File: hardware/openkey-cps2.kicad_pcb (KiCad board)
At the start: 2 copper layers, 27.4 x 27.2 mm, 19 parts, among them CN9 Conn_01x06, J1 VCC Pad, J2 CN2, J3 GND Pad, J4 VCC, J5 GND, J6 J5 / UDPI, U1 ATtinyxx4

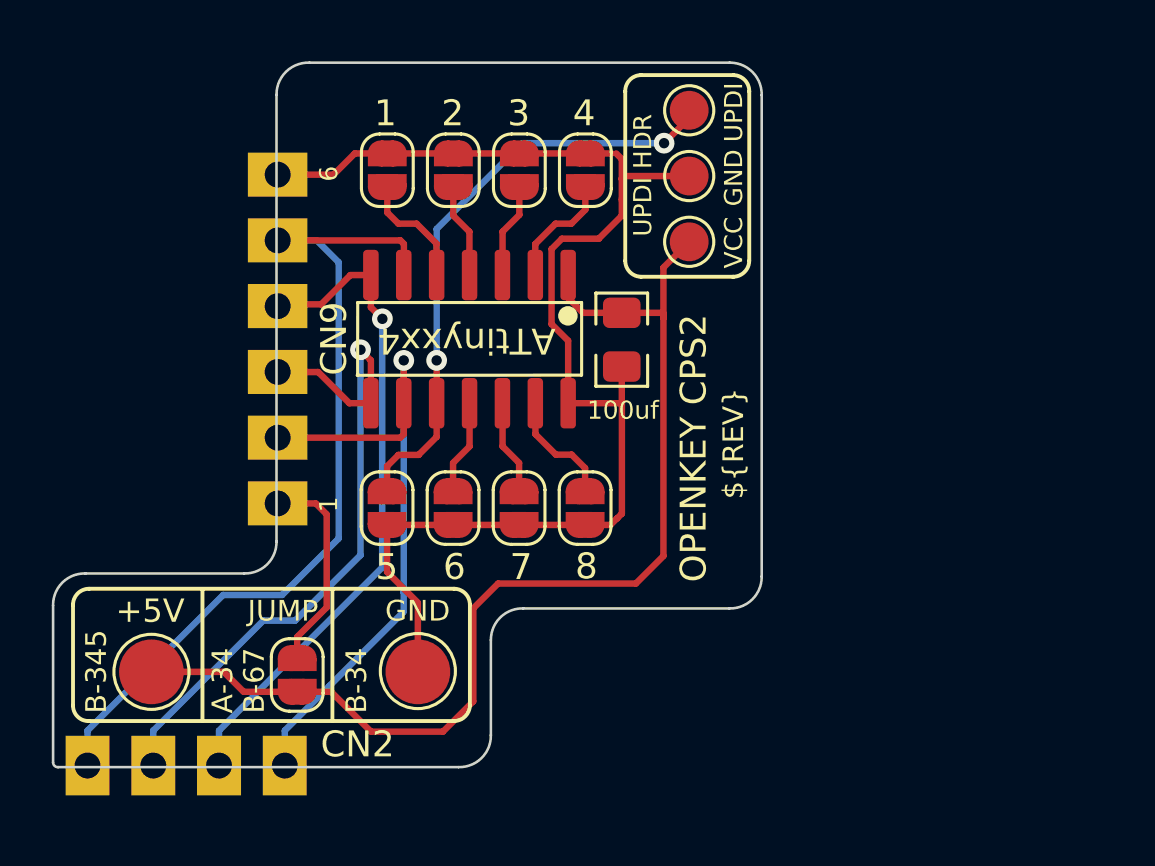
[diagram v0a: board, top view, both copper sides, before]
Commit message: HW: get most everything 0.25mm aligned
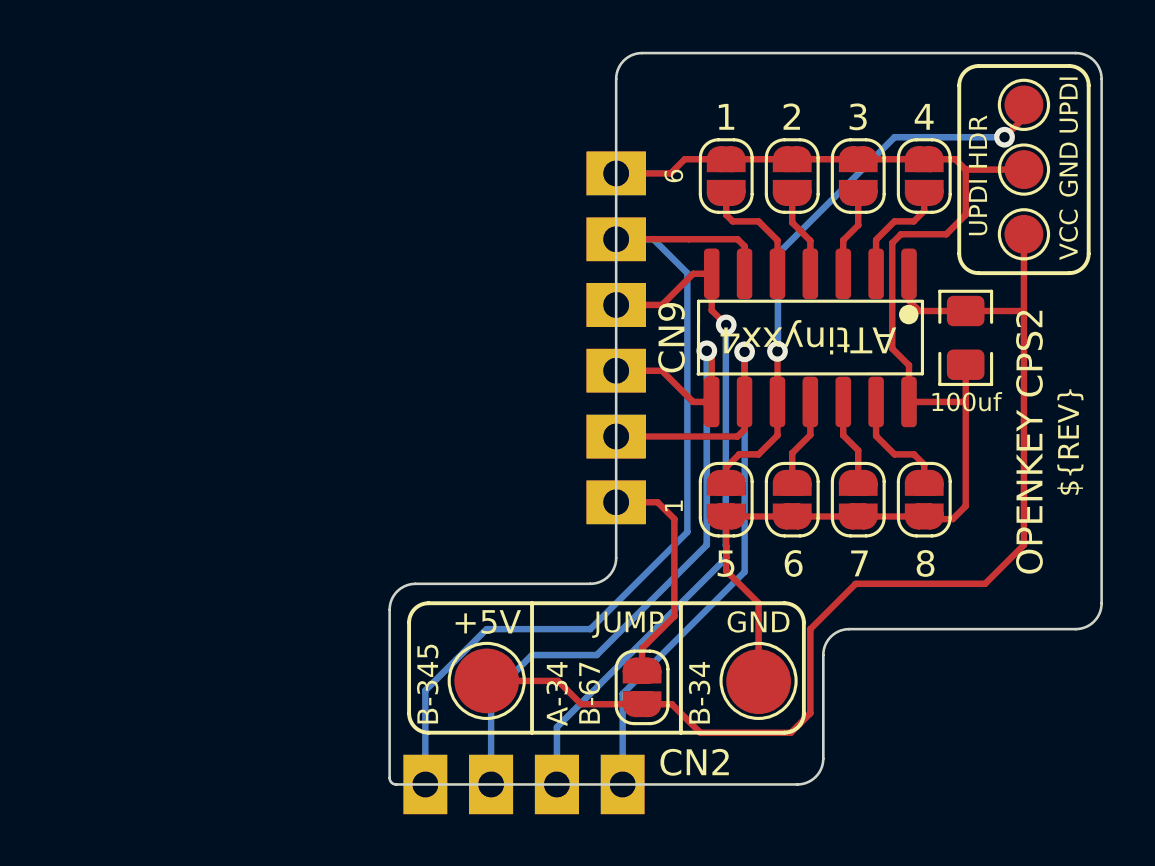
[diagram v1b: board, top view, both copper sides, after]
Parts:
- moved JP9 13.3 mm to (134.0, 110.8)
- moved C1 13.3 mm to (146.5, 97.2)
- moved J3 13.2 mm to (138.5, 110.5)
- moved U1 13.2 mm to (140.5, 97.2)
- moved REF** 13.1 mm to (143.0, 98.0)
- moved JP2 13.1 mm to (139.8, 103.5)
- moved JP1 13.1 mm to (137.2, 103.5)
- moved JP3 13.1 mm to (142.3, 103.5)
- moved JP4 13.1 mm to (144.9, 103.5)
- moved JP7 13.1 mm to (139.8, 91.0)
- moved JP5 13.1 mm to (144.9, 91.0)
- moved JP6 13.1 mm to (142.3, 91.0)
- moved JP8 13.1 mm to (137.2, 91.0)
- moved CN9 13.1 mm to (133.0, 103.6)
- moved J2 13.1 mm to (133.2, 114.5)
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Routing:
- net RESET: track 32.5 -> 35.3 mm
- net GND: track 50.0 -> 51.5 mm
- net SETUP: track 26.3 -> 27.7 mm
- net DATA: track 25.2 -> 26.5 mm
- net VCC: track 43.2 -> 44.1 mm
- net /J5 / UPDI: track 23.2 -> 22.3 mm
- net CLOCK: track 25.7 -> 26.6 mm
- net /CN9 VCC: track 8.01 -> 8.76 mm
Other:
- board size 27.4 x 27.2 mm -> 27.5 x 28.2 mm

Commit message: HW: tweak so a VCC trace isn't so close to edge
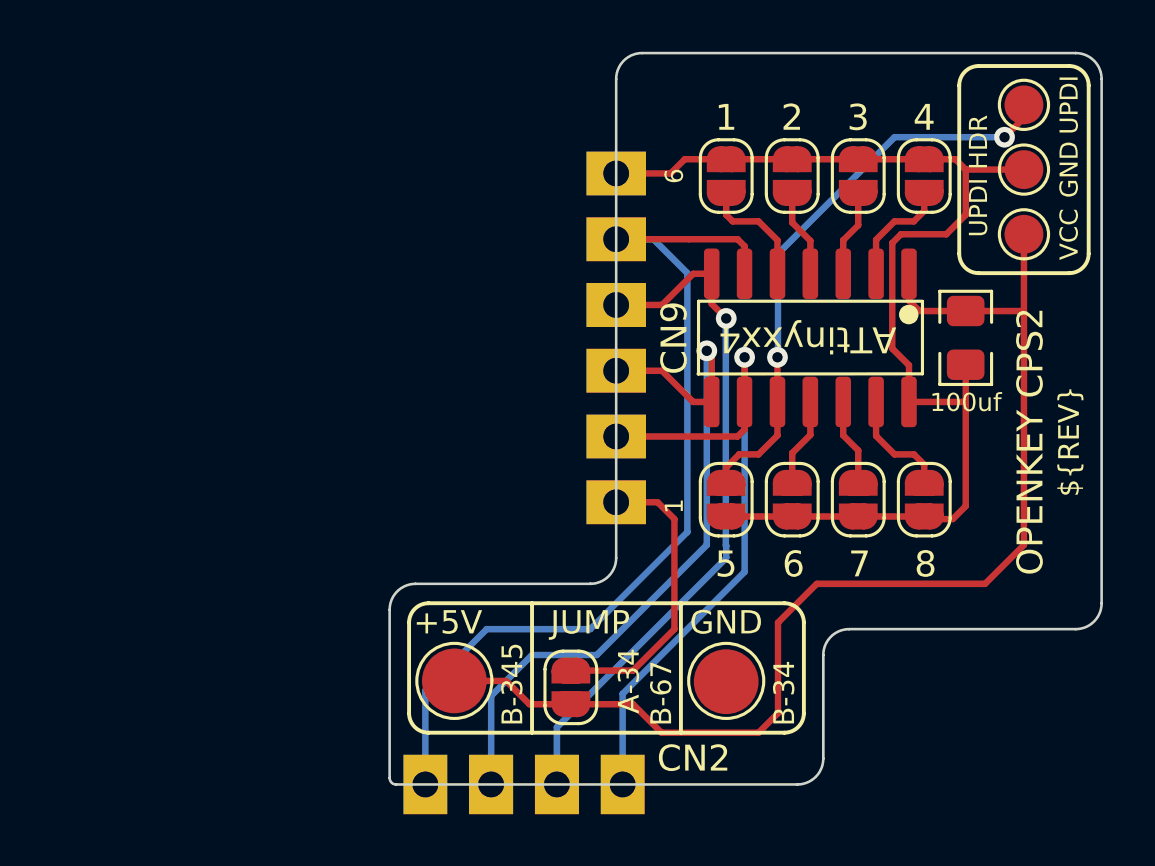
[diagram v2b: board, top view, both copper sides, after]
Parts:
- moved JP9 2.75 mm to (131.2, 110.8)
- moved J1 1.25 mm to (126.8, 110.5)
- moved J3 1.25 mm to (137.2, 110.5)
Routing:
- net GND: track 51.5 -> 44.6 mm
- net /CN9 VCC: track 8.76 -> 11.3 mm
- net VCC: track 44.1 -> 45.5 mm
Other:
- board text added: "CN9"

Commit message: HW: somehow missed connecting the ground pad, doh
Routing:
- net GND: track 44.6 -> 51.0 mm
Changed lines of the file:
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@@
     )
   )
-  (property "REV" "2022-12-07")
+  (property "REV" "2022-12-17")
   (net 0 "")
   (net 1 "VCC")
@@
   (segment (start 135.1 90.9) (end 133.125 90.9) (width 0.25) (layer "F.Cu") (net 2))
   (segment (start 143.665 97.665) (end 143.665 93.585) (width 0.25) (layer "F.Cu") (net 2))
+  (segment (start 137.25 104.15) (end 137.25 110.53) (width 0.25) (layer "F.Cu") (net 2))
   (segment (start 139.8 104.15) (end 137.25 104.15) (width 0.25) (layer "F.Cu") (net 2))
   (segment (start 145 104.25) (end 146 104.25) (width 0.25) (layer "F.Cu") (net 2))

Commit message: HW: bypass cap value typo'd as 100uf when it should be 100nf
Thanks for hatmoose for pointing out the typo
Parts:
- C1: value 100uf -> 100nf
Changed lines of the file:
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@@
     )
   )
-  (property "REV" "2022-12-17")
+  (property "REV" "2023-01-03")
   (net 0 "")
   (net 1 "VCC")
@@
       (effects (font (size 0.7 0.7) (thickness 0.12)))
     )
-    (fp_text value "100uf" (at -2.5 0) (layer "F.SilkS")
+    (fp_text value "100nf" (at -2.5 0) (layer "F.SilkS")
       (effects (font (size 0.7 0.7) (thickness 0.12)))
     )

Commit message: panel + assembly updates
- have kikit create the panel (was done by hand before)
- have jlcpcb fabrication plugin create bom/positions files for the panel
- create PANEL.md with instructions for having jlcpcb assemble the board
- update kicad files to 10.x
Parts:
- added REF**: Tab, PCM_kikit:Tab, F.Cu at (146.0, 108.6)
- added REF**: Tab, PCM_kikit:Tab, F.Cu at (146.0, 86.2)
